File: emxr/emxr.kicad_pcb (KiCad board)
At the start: 2 copper layers, 1 part, among them SW1 Audio Selector

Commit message: finish footprints, starting on component placement
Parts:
- removed SW1: Audio Selector, dba_footprint:CK1050
- added C201: 0.01, Capacitor_THT:C_Disc_D3.8mm_W2.6mm_P2.50mm, F.Cu at (264.2, 22.9)
- added C202: 0.01, Capacitor_THT:C_Disc_D3.8mm_W2.6mm_P2.50mm, F.Cu at (256.5, 39.4)
- added C203: 100p, Capacitor_THT:C_Disc_D5.0mm_W2.5mm_P2.50mm, F.Cu at (252.7, 31.1)
- added C204: 100p, Capacitor_THT:C_Disc_D5.0mm_W2.5mm_P2.50mm, F.Cu at (237.5, 33.0)
- added C205: 22/50, Capacitor_THT:CP_Radial_D5.0mm_P2.00mm, F.Cu at (239.7, 37.5)
- added C206: 22/50, Capacitor_THT:CP_Radial_D5.0mm_P2.00mm, F.Cu at (256.5, 24.5)
- added C207: 100p, Capacitor_THT:C_Disc_D5.0mm_W2.5mm_P2.50mm, F.Cu at (267.3, 33.6)
- added C208: 100p, Capacitor_THT:C_Disc_D5.0mm_W2.5mm_P2.50mm, F.Cu at (276.9, 41.3)
- added C209: 22/50, Capacitor_THT:CP_Radial_D5.0mm_P2.00mm, F.Cu at (269.2, 47.9)
- added C210: 22/50, Capacitor_THT:CP_Radial_D5.0mm_P2.00mm, F.Cu at (269.2, 27.0)
- added C301: 0.1, Capacitor_THT:C_Disc_D3.8mm_W2.6mm_P2.50mm, F.Cu at (250.4, 138.4)
- added C302: 100/25, Capacitor_THT:CP_Radial_D8.0mm_P3.50mm, F.Cu at (256.9, 136.7)
- added C303: 0.1, Capacitor_THT:C_Disc_D3.8mm_W2.6mm_P2.50mm, F.Cu at (239.0, 147.3)
- added C304: 100/25, Capacitor_THT:CP_Radial_D8.0mm_P3.50mm, F.Cu at (231.0, 151.9)
- added C305: 100p, Capacitor_THT:C_Disc_D5.0mm_W2.5mm_P2.50mm, F.Cu at (235.7, 139.2)
- added C306: 22/50, Capacitor_THT:CP_Radial_D5.0mm_P2.00mm, F.Cu at (232.7, 159.1)
- added C307: 220/25, Capacitor_THT:CP_Radial_D10.0mm_P5.00mm, F.Cu at (229.1, 122.7)
- added C308: 100p, Capacitor_THT:C_Disc_D5.0mm_W2.5mm_P2.50mm, F.Cu at (216.9, 149.4)
- added C309: 100p, Capacitor_THT:C_Disc_D5.0mm_W2.5mm_P2.50mm, F.Cu at (235.7, 142.7)
- added C311: 0.001, Capacitor_THT:C_Disc_D3.8mm_W2.6mm_P2.50mm, F.Cu at (239.8, 116.6)
- added C312: 100p, Capacitor_THT:C_Disc_D5.0mm_W2.5mm_P2.50mm, F.Cu at (250.4, 143.8)
- added C313: 22/50, Capacitor_THT:CP_Radial_D5.0mm_P2.00mm, F.Cu at (261.1, 158.6)
- added C314: 220/25, Capacitor_THT:CP_Radial_D10.0mm_P5.00mm, F.Cu at (257.6, 120.7)
- added C315: 100p, Capacitor_THT:C_Disc_D5.0mm_W2.5mm_P2.50mm, F.Cu at (268.2, 139.4)
- added C316: 100p, Capacitor_THT:C_Disc_D5.0mm_W2.5mm_P2.50mm, F.Cu at (247.9, 147.3)
- added C318: 0.001, Capacitor_THT:C_Disc_D3.8mm_W2.6mm_P2.50mm, F.Cu at (246.9, 116.6)
- added C401: 0.01, Capacitor_THT:C_Disc_D3.8mm_W2.6mm_P2.50mm, F.Cu at (66.9, -80.1)
- added C402: 0.01, Capacitor_THT:C_Disc_D3.8mm_W2.6mm_P2.50mm, F.Cu at (29.8, -42.0)
- added C403: 0.01, Capacitor_THT:C_Disc_D3.8mm_W2.6mm_P2.50mm, F.Cu at (51.0, -63.0)
- added C404: 0.01, Capacitor_THT:C_Disc_D3.8mm_W2.6mm_P2.50mm, F.Cu at (45.4, -60.9)
- added C405: 0.01, Capacitor_THT:C_Disc_D3.8mm_W2.6mm_P2.50mm, F.Cu at (57.1, -71.2)
- added C406: 0.01, Capacitor_THT:C_Disc_D3.8mm_W2.6mm_P2.50mm, F.Cu at (41.6, -54.3)
- added C407: 0.01, Capacitor_THT:C_Disc_D3.8mm_W2.6mm_P2.50mm, F.Cu at (30.0, -46.2)
- added C408: 0.01, Capacitor_THT:C_Disc_D3.8mm_W2.6mm_P2.50mm, F.Cu at (56.7, -67.0)
- added C409: 47p, Capacitor_THT:C_Disc_D3.8mm_W2.6mm_P2.50mm, F.Cu at (50.5, -67.1)
- added C410: 150p, Capacitor_THT:C_Disc_D5.0mm_W2.5mm_P2.50mm, F.Cu at (23.7, -42.2)
- added C411: 150p, Capacitor_THT:C_Disc_D5.0mm_W2.5mm_P2.50mm, F.Cu at (17.1, -42.2)
- added C412: 220/25, Capacitor_THT:CP_Radial_D10.0mm_P5.00mm, F.Cu at (40.7, -68.7)
- added C413: 22/50, Capacitor_THT:CP_Radial_D5.0mm_P2.00mm, F.Cu at (24.1, -47.5)
- added C414: 22/50, Capacitor_THT:CP_Radial_D5.0mm_P2.00mm, F.Cu at (54.4, -83.0)
- added C415: 22/50, Capacitor_THT:CP_Radial_D5.0mm_P2.00mm, F.Cu at (54.4, -76.5)
- added C416: 220p, Capacitor_THT:C_Disc_D5.0mm_W2.5mm_P2.50mm, F.Cu at (60.7, -77.8)
- added C417: 47/50, Capacitor_THT:CP_Radial_D6.3mm_P2.50mm, F.Cu at (28.3, -58.4)
- added C418: 100p, Capacitor_THT:C_Disc_D5.0mm_W2.5mm_P2.50mm, F.Cu at (30.4, -50.3)
- added C420: 47p, Capacitor_THT:C_Disc_D3.8mm_W2.6mm_P2.50mm, F.Cu at (66.9, -84.2)
- added C421: 150p, Capacitor_THT:C_Disc_D5.0mm_W2.5mm_P2.50mm, F.Cu at (51.0, -71.2)
- added C422: 150p, Capacitor_THT:C_Disc_D5.0mm_W2.5mm_P2.50mm, F.Cu at (-10.9, -40.0)
- added C423: 220/25, Capacitor_THT:CP_Radial_D10.0mm_P5.00mm, F.Cu at (17.2, -56.5)
- added C424: 22/50, Capacitor_THT:CP_Radial_D5.0mm_P2.00mm, F.Cu at (61.0, -83.0)
- added C425: 22/50, Capacitor_THT:CP_Radial_D5.0mm_P2.00mm, F.Cu at (17.5, -47.5)
- added C426: 22/50, Capacitor_THT:CP_Radial_D5.0mm_P2.00mm, F.Cu at (39.5, -59.6)
- added C427: 220p, Capacitor_THT:C_Disc_D5.0mm_W2.5mm_P2.50mm, F.Cu at (35.5, -54.4)
- added C428: 47/50, Capacitor_THT:CP_Radial_D6.3mm_P2.50mm, F.Cu at (9.96, -42.2)
- added C429: 100p, Capacitor_THT:C_Disc_D5.1mm_W3.2mm_P5.00mm, F.Cu at (0.57, -43.8)
- added FR301: 10 1/4, Resistor_THT:R_Axial_DIN0207_L6.3mm_D2.5mm_P5.08mm_Vertical, F.Cu at (258.9, 130.6)
- added FR302: 10 1/4, Resistor_THT:R_Axial_DIN0207_L6.3mm_D2.5mm_P5.08mm_Vertical, F.Cu at (244.1, 151.9)
- added IC201: NJM4558D, Package_DIP:DIP-8_W7.62mm_Socket_LongPads, F.Cu at (256.5, 28.6)
- added IC301: NJM4556D, Package_DIP:DIP-8_W7.62mm_Socket_LongPads, F.Cu at (239.5, 136.4)
- added IC401: NJM2068DD, Package_DIP:DIP-8_W7.62mm_Socket_LongPads, F.Cu at (15.7, -72.0)
- added IC402: NJM4580, Package_DIP:DIP-8_W7.62mm_Socket_LongPads, F.Cu at (42.4, -84.2)
- added IC403: NJM2068DD, Package_DIP:DIP-8_W7.62mm_Socket_LongPads, F.Cu at (27.5, -72.0)
- added IC404: NJM4580, Package_DIP:DIP-8_W7.62mm_Socket_LongPads, F.Cu at (2.43, -55.9)
- added J101: POWER, Connector_JST:JST_XH_B4B-XH-A_1x04_P2.50mm_Vertical, F.Cu at (-18.5, -117.4)
- added J102: DSP_PW, Connector_JST:JST_XH_B5B-XH-A_1x05_P2.50mm_Vertical, F.Cu at (-35.5, -117.4)
- added J103: Bus Conn, Connector_PinHeader_2.54mm:PinHeader_1x12_P2.54mm_Vertical, F.Cu at (-41.3, -118.4)
- added J104: GEQ_L_PRE, Connector_JST:JST_XH_B3B-XH-A_1x03_P2.50mm_Vertical, F.Cu at (-4.08, -117.4)
- added J105: GEQ_L_POST, Connector_JST:JST_XH_B3B-XH-A_1x03_P2.50mm_Vertical, F.Cu at (-35.5, -101.8)
- added J106: GEQ_R_PRE, Connector_JST:JST_XH_B2B-XH-A_1x02_P2.50mm_Vertical, F.Cu at (-35.5, -94.0)
- added J107: GEQ_R_POST, Connector_JST:JST_XH_B2B-XH-A_1x02_P2.50mm_Vertical, F.Cu at (-23.5, -101.8)
- added J108: AUDIO_OUT, Connector_JST:JST_XH_B4B-XH-A_1x04_P2.50mm_Vertical, F.Cu at (-35.5, -109.6)
- added J201: RCA_IN_A_B, Connector_JST:JST_XH_B6B-XH-A_1x06_P2.50mm_Vertical, F.Cu at (-44.7, 42.0)
- added J202: RCA_IN_3_4, Connector_JST:JST_XH_B6B-XH-A_1x06_P2.50mm_Vertical, F.Cu at (-45.6, 73.3)
- added J203: AUX1_IN, Connector_JST:JST_XH_B3B-XH-A_1x03_P2.50mm_Vertical, F.Cu at (-44.4, 91.9)
- added J204: AUX2_IN, Connector_JST:JST_XH_B3B-XH-A_1x03_P2.50mm_Vertical, F.Cu at (-45.7, 84.9)
- added J205: InpVolL, Connector_JST:JST_XH_B3B-XH-A_1x03_P2.50mm_Vertical, F.Cu at (232.4, 32.5)
- added J206: InpVolR, Connector_JST:JST_XH_B2B-XH-A_1x02_P2.50mm_Vertical, F.Cu at (271.7, 40.6)
- added J207: SrcInL, Connector_JST:JST_XH_B6B-XH-A_1x06_P2.50mm_Vertical, F.Cu at (-36.1, 61.0)
- added J208: SrcSel, Connector_JST:JST_XH_B2B-XH-A_1x02_P2.50mm_Vertical, F.Cu at (247.7, 42.5)
- added J209: SrcInR, Connector_JST:JST_XH_B6B-XH-A_1x06_P2.50mm_Vertical, F.Cu at (-36.1, 41.3)
- added J301: HPHONES, Connector_JST:JST_XH_B3B-XH-A_1x03_P2.50mm_Vertical, F.Cu at (240.8, 108.7)
- added J302: HPVolL, Connector_JST:JST_XH_B3B-XH-A_1x03_P2.50mm_Vertical, F.Cu at (243.8, 160.5)
- added J303: HPVolR, Connector_JST:JST_XH_B2B-XH-A_1x02_P2.50mm_Vertical, F.Cu at (252.0, 159.5)
- added J401: FrontVolL, Connector_JST:JST_XH_B3B-XH-A_1x03_P2.50mm_Vertical, F.Cu at (30.4, -78.9)
- added J402: FrontVolR, Connector_JST:JST_XH_B3B-XH-A_1x03_P2.50mm_Vertical, F.Cu at (-9.48, -46.5)
- added LC301: 270p, dba_footprint:LCL_EMX, F.Cu at (236.2, 111.3)
- added LC302: 270p, dba_footprint:LCL_EMX, F.Cu at (250.4, 111.3)
- added R101: 10, Resistor_THT:R_Axial_DIN0207_L6.3mm_D2.5mm_P10.16mm_Horizontal, F.Cu at (-42.0, -86.1)
- added R102: 10, Resistor_THT:R_Axial_DIN0207_L6.3mm_D2.5mm_P10.16mm_Horizontal, F.Cu at (-22.9, -110.9)
- added R201: 15k, Resistor_THT:R_Axial_DIN0207_L6.3mm_D2.5mm_P10.16mm_Horizontal, F.Cu at (239.4, 29.8)
- added R202: 100, Resistor_THT:R_Axial_DIN0207_L6.3mm_D2.5mm_P10.16mm_Horizontal, F.Cu at (222.2, 29.8)
- added R203: 47k, Resistor_THT:R_Axial_DIN0207_L6.3mm_D2.5mm_P10.16mm_Horizontal, F.Cu at (226.1, 40.0)
- added R204: 100, Resistor_THT:R_Axial_DIN0207_L6.3mm_D2.5mm_P10.16mm_Horizontal, F.Cu at (243.2, 37.5)
- added R205: 27k, Resistor_THT:R_Axial_DIN0207_L6.3mm_D2.5mm_P10.16mm_Horizontal, F.Cu at (246.4, 15.9)
- added R206: 47k, Resistor_THT:R_Axial_DIN0207_L6.3mm_D2.5mm_P10.16mm_Horizontal, F.Cu at (256.5, 19.1)
- added R207: 10k, Resistor_THT:R_Axial_DIN0207_L6.3mm_D2.5mm_P10.16mm_Horizontal, F.Cu at (239.4, 26.0)
- added R208: 18k, Resistor_THT:R_Axial_DIN0207_L6.3mm_D2.5mm_P10.16mm_Horizontal, F.Cu at (253.4, 34.3)
- added R209: 15k, Resistor_THT:R_Axial_DIN0207_L6.3mm_D2.5mm_P10.16mm_Horizontal, F.Cu at (280.7, 31.1)
- added R210: 100, Resistor_THT:R_Axial_DIN0207_L6.3mm_D2.5mm_P10.16mm_Horizontal, F.Cu at (273.7, 45.1)
- added R211: 47k, Resistor_THT:R_Axial_DIN0207_L6.3mm_D2.5mm_P10.16mm_Horizontal, F.Cu at (276.9, 55.2)
- added R212: 100, Resistor_THT:R_Axial_DIN0207_L6.3mm_D2.5mm_P10.16mm_Horizontal, F.Cu at (264.2, 49.5)
- added R213: 27k, Resistor_THT:R_Axial_DIN0207_L6.3mm_D2.5mm_P10.16mm_Horizontal, F.Cu at (259.1, 19.1)
- added R214: 18k, Resistor_THT:R_Axial_DIN0207_L6.3mm_D2.5mm_P10.16mm_Horizontal, F.Cu at (261.0, 39.4)
- added R215: 47k, Resistor_THT:R_Axial_DIN0207_L6.3mm_D2.5mm_P10.16mm_Horizontal, F.Cu at (269.2, 15.8)
- added R216: 10k, Resistor_THT:R_Axial_DIN0207_L6.3mm_D2.5mm_P10.16mm_Horizontal, F.Cu at (280.7, 34.9)
- added R301: 10k, Resistor_THT:R_Axial_DIN0207_L6.3mm_D2.5mm_P10.16mm_Horizontal, F.Cu at (231.6, 146.3)
- added R302: 100, Resistor_THT:R_Axial_DIN0207_L6.3mm_D2.5mm_P10.16mm_Horizontal, F.Cu at (235.7, 165.6)
- added R303: 220, Resistor_THT:R_Axial_DIN0207_L6.3mm_D2.5mm_P10.16mm_Horizontal, F.Cu at (220.5, 136.1)
- added R304: 220, Resistor_THT:R_Axial_DIN0207_L6.3mm_D2.5mm_P10.16mm_Horizontal, F.Cu at (224.0, 146.3)
- added R305: 100/1W, Resistor_THT:R_Axial_DIN0207_L6.3mm_D2.5mm_P15.24mm_Horizontal, F.Cu at (236.2, 133.1)
- added R306: 18k, Resistor_THT:R_Axial_DIN0207_L6.3mm_D2.5mm_P10.16mm_Horizontal, F.Cu at (216.9, 146.3)
- added R307: 100k, Resistor_THT:R_Axial_DIN0207_L6.3mm_D2.5mm_P10.16mm_Horizontal, F.Cu at (239.8, 118.9)
- added R308: 10k, Resistor_THT:R_Axial_DIN0207_L6.3mm_D2.5mm_P10.16mm_Horizontal, F.Cu at (227.6, 146.3)
- added R309: 10k, Resistor_THT:R_Axial_DIN0207_L6.3mm_D2.5mm_P10.16mm_Horizontal, F.Cu at (254.0, 152.4)
- added R310: 100, Resistor_THT:R_Axial_DIN0207_L6.3mm_D2.5mm_P10.16mm_Horizontal, F.Cu at (248.9, 165.6)
- added R311: 220, Resistor_THT:R_Axial_DIN0207_L6.3mm_D2.5mm_P10.16mm_Horizontal, F.Cu at (264.7, 152.4)
- added R312: 220, Resistor_THT:R_Axial_DIN0207_L6.3mm_D2.5mm_P10.16mm_Horizontal, F.Cu at (261.1, 142.2)
- added R313: 100/1W, Resistor_THT:R_Axial_DIN0207_L6.3mm_D2.5mm_P15.24mm_Horizontal, F.Cu at (250.4, 133.1)
- added R314: 18k, Resistor_THT:R_Axial_DIN0207_L6.3mm_D2.5mm_P10.16mm_Horizontal, F.Cu at (268.2, 142.2)
- added R315: 100k, Resistor_THT:R_Axial_DIN0207_L6.3mm_D2.5mm_P10.16mm_Horizontal, F.Cu at (246.9, 118.9)
- added R316: 10k, Resistor_THT:R_Axial_DIN0207_L6.3mm_D2.5mm_P10.16mm_Horizontal, F.Cu at (257.6, 152.4)
- added R401: 27k, Resistor_THT:R_Axial_DIN0207_L6.3mm_D2.5mm_P10.16mm_Horizontal, F.Cu at (1.93, -64.0)
- added R402: 10k, Resistor_THT:R_Axial_DIN0207_L6.3mm_D2.5mm_P10.16mm_Horizontal, F.Cu at (15.2, -80.2)
- added R403: 11k, Resistor_THT:R_Axial_DIN0207_L6.3mm_D2.5mm_P10.16mm_Horizontal, F.Cu at (-11.4, -51.9)
- added R404: 10k, Resistor_THT:R_Axial_DIN0207_L6.3mm_D2.5mm_P10.16mm_Horizontal, F.Cu at (-11.4, -60.0)
- added R405: 100k, Resistor_THT:R_Axial_DIN0207_L6.3mm_D2.5mm_P10.16mm_Horizontal, F.Cu at (15.2, -84.3)
- added R406: 100, Resistor_THT:R_Axial_DIN0207_L6.3mm_D2.5mm_P10.16mm_Horizontal, F.Cu at (1.93, -76.2)
- added R407: 330, Resistor_THT:R_Axial_DIN0207_L6.3mm_D2.5mm_P10.16mm_Horizontal, F.Cu at (1.93, -72.2)
- added R408: 10, Resistor_THT:R_Axial_DIN0207_L6.3mm_D2.5mm_P10.16mm_Horizontal, F.Cu at (1.93, -84.3)
- added R409: 47k, Resistor_THT:R_Axial_DIN0207_L6.3mm_D2.5mm_P10.16mm_Horizontal, F.Cu at (1.93, -68.1)
- added R410: 15k, Resistor_THT:R_Axial_DIN0207_L6.3mm_D2.5mm_P10.16mm_Horizontal, F.Cu at (-11.4, -76.2)
- added R411: 27k, Resistor_THT:R_Axial_DIN0207_L6.3mm_D2.5mm_P10.16mm_Horizontal, F.Cu at (1.93, -80.2)
- added R412: 10k, Resistor_THT:R_Axial_DIN0207_L6.3mm_D2.5mm_P10.16mm_Horizontal, F.Cu at (28.6, -84.3)
- added R413: 11k, Resistor_THT:R_Axial_DIN0207_L6.3mm_D2.5mm_P10.16mm_Horizontal, F.Cu at (-11.4, -56.0)
- added R414: 10k, Resistor_THT:R_Axial_DIN0207_L6.3mm_D2.5mm_P10.16mm_Horizontal, F.Cu at (15.2, -76.2)
- added R415: 100k, Resistor_THT:R_Axial_DIN0207_L6.3mm_D2.5mm_P10.16mm_Horizontal, F.Cu at (-11.4, -64.0)
- added R416: 100, Resistor_THT:R_Axial_DIN0207_L6.3mm_D2.5mm_P10.16mm_Horizontal, F.Cu at (-11.4, -68.1)
- added R417: 330, Resistor_THT:R_Axial_DIN0207_L6.3mm_D2.5mm_P10.16mm_Horizontal, F.Cu at (-11.4, -80.2)
- added R418: 10, Resistor_THT:R_Axial_DIN0207_L6.3mm_D2.5mm_P10.16mm_Horizontal, F.Cu at (-11.4, -84.3)
- added R419: 47k, Resistor_THT:R_Axial_DIN0207_L6.3mm_D2.5mm_P10.16mm_Horizontal, F.Cu at (1.93, -60.0)
- added R420: 15k, Resistor_THT:R_Axial_DIN0207_L6.3mm_D2.5mm_P10.16mm_Horizontal, F.Cu at (-11.4, -72.2)
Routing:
- added copper zone on B.Cu, net GND
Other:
- board text removed: "BACK"
- board text removed: "FRONT"

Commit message: progress on layouting
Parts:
- moved J106 331.9 mm to (246.9, 80.5)
- moved J101 275.3 mm to (52.8, 148.5), turned to 90 degrees
- moved J104 249.6 mm to (144.3, 83.4), turned to -90 degrees
- moved C424 240.8 mm to (262.9, 48.3)
- moved C427 240.8 mm to (237.4, 77.0)
- moved C403 240.8 mm to (252.9, 68.4)
- moved C404 240.8 mm to (247.2, 70.5)
- moved C407 240.8 mm to (231.8, 85.1)
- moved C408 240.8 mm to (258.6, 64.3)
- moved C420 240.8 mm to (268.8, 47.1)
- moved C421 240.8 mm to (252.9, 60.1)
- moved C422 240.8 mm to (190.9, 91.3)
- moved C425 240.8 mm to (219.4, 83.8)
- moved C426 240.8 mm to (241.4, 71.7)
- moved C428 240.8 mm to (211.8, 89.1)
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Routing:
- net Net-(C411-Pad1): track 0.00 -> 30.0 mm
- net SINGAL_L_PRE_GEQ: track 0.00 -> 29.5 mm
- net Net-(C410-Pad2): track 0.00 -> 28.2 mm
- net Net-(C418-Pad1): track 0.00 -> 24.5 mm
- net Net-(C409-Pad1): track 0.00 -> 23.1 mm
- net Net-(C410-Pad1): track 0.00 -> 17.8 mm
- net Net-(C411-Pad2): track 0.00 -> 16.7 mm
- net Net-(C409-Pad2): track 0.00 -> 13.1 mm
- net /Stereo/POT_FRONT_VOL_L_PRE: track 0.00 -> 9.42 mm
- net /Stereo/POT_FRONT_VOL_L_POST: track 0.00 -> 9.18 mm
- net -15V: track 0.00 -> 6.73 mm
- net +15V: track 0.00 -> 6.60 mm
- net Net-(C415-Pad1): track 0.00 -> 6.39 mm
- net Net-(C417-Pad2): track 0.00 -> 6.14 mm
- net Net-(C417-Pad1): track 0.00 -> 5.98 mm
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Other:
- board text added: "JLCJLCJLCJLC"

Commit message: replicated layout
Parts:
- removed C403, C404, C407, C408: 0.01, Capacitor_THT:C_Disc_D3.8mm_W2.6mm_P2.50mm
- removed C420: 47p, Capacitor_THT:C_Disc_D3.8mm_W2.6mm_P2.50mm
- removed C421, C422: 150p, Capacitor_THT:C_Disc_D5.0mm_W2.5mm_P2.50mm
- removed C423: 220/25, Capacitor_THT:CP_Radial_D10.0mm_P5.00mm
- removed C424, C425, C426: 22/50, Capacitor_THT:CP_Radial_D5.0mm_P2.00mm
- removed C427: 220p, Capacitor_THT:C_Disc_D5.0mm_W2.5mm_P2.50mm
- removed C428: 47/50, Capacitor_THT:CP_Radial_D6.3mm_P2.50mm
- removed C429: 100p, Capacitor_THT:C_Disc_D5.1mm_W3.2mm_P5.00mm
- removed IC403: NJM2068DD, Package_DIP:DIP-8_W7.62mm_Socket_LongPads
- removed IC404: NJM4580, Package_DIP:DIP-8_W7.62mm_Socket_LongPads
- removed J402: FrontVolR, Connector_JST:JST_XH_B3B-XH-A_1x03_P2.50mm_Vertical
- removed R411: 27k, Resistor_THT:R_Axial_DIN0207_L6.3mm_D2.5mm_P10.16mm_Horizontal
- removed R412, R414: 10k, Resistor_THT:R_Axial_DIN0207_L6.3mm_D2.5mm_P10.16mm_Horizontal
- removed R413: 11k, Resistor_THT:R_Axial_DIN0207_L6.3mm_D2.5mm_P10.16mm_Horizontal
- removed R415: 100k, Resistor_THT:R_Axial_DIN0207_L6.3mm_D2.5mm_P10.16mm_Horizontal
- removed R416: 100, Resistor_THT:R_Axial_DIN0207_L6.3mm_D2.5mm_P10.16mm_Horizontal
- removed R417: 330, Resistor_THT:R_Axial_DIN0207_L6.3mm_D2.5mm_P10.16mm_Horizontal
- removed R418: 10, Resistor_THT:R_Axial_DIN0207_L6.3mm_D2.5mm_P10.16mm_Horizontal
- removed R419: 47k, Resistor_THT:R_Axial_DIN0207_L6.3mm_D2.5mm_P10.16mm_Horizontal
- removed R420: 15k, Resistor_THT:R_Axial_DIN0207_L6.3mm_D2.5mm_P10.16mm_Horizontal
- added C501: 0.01, Capacitor_THT:C_Disc_D3.8mm_W2.6mm_P2.50mm, F.Cu at (199.7, 124.5)
- added C502: 0.01, Capacitor_THT:C_Disc_D3.8mm_W2.6mm_P2.50mm, F.Cu at (218.0, 120.9)
- added C503: 0.01, Capacitor_THT:C_Disc_D3.8mm_W2.6mm_P2.50mm, F.Cu at (194.6, 110.2)
- added C504: 0.01, Capacitor_THT:C_Disc_D3.8mm_W2.6mm_P2.50mm, F.Cu at (212.6, 106.7)
- added C505: 47p, Capacitor_THT:C_Disc_D3.8mm_W2.6mm_P2.50mm, F.Cu at (199.7, 110.2)
- added C506: 150p, Capacitor_THT:C_Disc_D5.0mm_W2.5mm_P2.50mm, F.Cu at (218.0, 106.7)
- added C507: 150p, Capacitor_THT:C_Disc_D5.0mm_W2.5mm_P2.50mm, F.Cu at (212.6, 120.9)
- added C508: 220/25, Capacitor_THT:CP_Radial_D10.0mm_P5.00mm, F.Cu at (187.7, 105.1)
- added C509: 22/50, Capacitor_THT:CP_Radial_D5.0mm_P2.00mm, F.Cu at (207.5, 116.0)
- added C510: 22/50, Capacitor_THT:CP_Radial_D5.0mm_P2.00mm, F.Cu at (239.8, 102.6)
- added C511: 22/50, Capacitor_THT:CP_Radial_D5.0mm_P2.00mm, F.Cu at (239.8, 110.7)
- added C512: 220p, Capacitor_THT:C_Disc_D5.0mm_W2.5mm_P2.50mm, F.Cu at (194.8, 104.9)
- added C513: 47/50, Capacitor_THT:CP_Radial_D6.3mm_P2.50mm, F.Cu at (240.3, 122.5)
- added C514: 100p, Capacitor_THT:C_Disc_D5.0mm_W2.5mm_P2.50mm, F.Cu at (206.8, 120.9)
- added IC501: NJM2068DD, Package_DIP:DIP-8_W7.62mm_Socket_LongPads, F.Cu at (202.2, 113.5)
- added IC502: NJM4580, Package_DIP:DIP-8_W7.62mm_Socket_LongPads, F.Cu at (220.5, 110.0)
- added J501: FrontVolL, Connector_JST:JST_XH_B3B-XH-A_1x03_P2.50mm_Vertical, F.Cu at (248.4, 106.5)
- added R501: 27k, Resistor_THT:R_Axial_DIN0207_L6.3mm_D2.5mm_P10.16mm_Horizontal, F.Cu at (193.0, 100.8)
- added R502: 10k, Resistor_THT:R_Axial_DIN0207_L6.3mm_D2.5mm_P10.16mm_Horizontal, F.Cu at (212.1, 100.8)
- added R503: 11k, Resistor_THT:R_Axial_DIN0207_L6.3mm_D2.5mm_P10.16mm_Horizontal, F.Cu at (234.4, 118.9)
- added R504: 10k, Resistor_THT:R_Axial_DIN0207_L6.3mm_D2.5mm_P10.16mm_Horizontal, F.Cu at (207.5, 111.0)
- added R505: 100, Resistor_THT:R_Axial_DIN0207_L6.3mm_D2.5mm_P10.16mm_Horizontal, F.Cu at (234.4, 108.2)
- added R506: 100k, Resistor_THT:R_Axial_DIN0207_L6.3mm_D2.5mm_P10.16mm_Horizontal, F.Cu at (234.4, 104.6)
- added R507: 330, Resistor_THT:R_Axial_DIN0207_L6.3mm_D2.5mm_P10.16mm_Horizontal, F.Cu at (224.3, 122.2)
- added R508: 10, Resistor_THT:R_Axial_DIN0207_L6.3mm_D2.5mm_P10.16mm_Horizontal, F.Cu at (234.4, 125.7)
- added R509: 47k, Resistor_THT:R_Axial_DIN0207_L6.3mm_D2.5mm_P10.16mm_Horizontal, F.Cu at (234.4, 111.8)
- added R510: 15k, Resistor_THT:R_Axial_DIN0207_L6.3mm_D2.5mm_P10.16mm_Horizontal, F.Cu at (234.4, 115.3)
- moved C204 150.5 mm to (169.0, -30.4)
- moved C208 150.5 mm to (208.4, -22.1)
- moved C209 150.5 mm to (200.8, -15.4)
- moved C210 150.5 mm to (200.8, -36.4)
- moved J206 150.5 mm to (203.3, -22.7)
- moved R202 150.5 mm to (153.8, -33.5)
- moved R203 150.5 mm to (157.6, -23.4)
- moved R205 150.5 mm to (177.9, -47.5)
- moved R208 150.5 mm to (184.9, -29.1)
- moved R209 150.5 mm to (212.2, -32.3)
- moved R210 150.5 mm to (205.2, -18.3)
- moved R211 150.5 mm to (208.4, -8.13)
- moved R214 150.5 mm to (192.5, -24.0)
- moved R215 150.5 mm to (200.8, -47.6)
- moved R216 150.5 mm to (212.2, -28.4)
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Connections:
- net /Stereo/POT_FRONT_VOL_L_POST renamed /Stereo Channel L/POT_FRONT_VOL_L_POST
- net /Stereo/POT_FRONT_VOL_L_PRE renamed /Stereo Channel L/POT_FRONT_VOL_L_PRE
- J201 pad 3: /Audio Selection/RCA_IN_A_R -> /Audio Selection/RCA_IN_B_L
- J201 pad 4: /Audio Selection/RCA_IN_B_L -> /Audio Selection/RCA_IN_A_R
- J202 pad 3: /Audio Selection/RCA_IN_C_R -> /Audio Selection/RCA_IN_D_L
- J202 pad 4: /Audio Selection/RCA_IN_D_L -> /Audio Selection/RCA_IN_C_R
- J207 pad 5: /Audio Selection/AUX_IN_L -> /Audio Selection/AUX1_IN_L
- J209 pad 5: /Audio Selection/AUX_IN_R -> /Audio Selection/AUX1_IN_R
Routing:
- net Net-(C507-Pad1): track 0.00 -> 30.0 mm
- net Net-(C506-Pad2): track 0.00 -> 28.2 mm
- net SINGAL_R_PRE_GEQ: track 0.00 -> 27.3 mm
- net Net-(C514-Pad1): track 0.00 -> 24.5 mm
- net Net-(C505-Pad1): track 0.00 -> 23.1 mm
- net Net-(C505-Pad2): track 0.00 -> 19.5 mm
- net Net-(C506-Pad1): track 0.00 -> 17.8 mm
- net Net-(C507-Pad2): track 0.00 -> 16.7 mm
- net /Stereo Channel R/POT_FRONT_VOL_L_PRE: track 0.00 -> 14.8 mm
- net /Stereo Channel R/POT_FRONT_VOL_L_POST: track 0.00 -> 9.18 mm
- net -15V: track 6.73 -> 13.5 mm
- net +15V: track 6.60 -> 13.2 mm
- net Net-(C511-Pad1): track 0.00 -> 6.39 mm
- net Net-(C409-Pad2): track 13.1 -> 19.5 mm
- net Net-(C513-Pad2): track 0.00 -> 6.14 mm
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
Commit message: more routing and reshuffling
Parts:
- removed J102: DSP_PW, Connector_JST:JST_XH_B5B-XH-A_1x05_P2.50mm_Vertical
- J103: footprint Connector_PinHeader_2.54mm:PinHeader_1x12_P2.54mm_Vertical -> Connector_JST:JST_XH_B6B-XH-A_1x06_P2.50mm_Vertical
- moved J103 321.2 mm to (117.0, 161.1), turned to 180 degrees
- moved R101 297.3 mm to (213.2, 66.3), turned to 180 degrees
- moved J105 295.9 mm to (211.9, 60.5)
- moved J108 288.8 mm to (198.0, 60.5)
- moved R102 277.3 mm to (190.3, 66.3)
- moved J107 267.4 mm to (189.1, 60.5)
- moved C206 205.4 mm to (113.0, 152.3)
- moved R206 204.9 mm to (113.0, 146.3), turned to 0 degrees
- moved J205 202.1 mm to (86.9, 155.9), turned to 90 degrees
- moved C201 198.2 mm to (93.5, 129.3), turned to 90 degrees
- moved R205 198.0 mm to (123.2, 142.7), turned to 180 degrees
- moved C205 196.7 mm to (96.8, 156.2)
- moved C204 196.7 mm to (93.7, 151.4), turned to 90 degrees
- moved R204 193.9 mm to (96.8, 151.6)
- moved R208 193.8 mm to (106.9, 148.3)
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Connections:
- J103 pad 2: +15VD -> -15V
- J103 pad 3: -15VD -> +15V
- J103 pad 4: GND -> BUS_R
- J103 pad 5: unconnected-(J103-Pad5) -> BUS_L
- J108 pad 1: SINGAL_L_POST_GEQ -> SINGAL_R_POST_GEQ
- J108 pad 3: SINGAL_R_POST_GEQ -> GND
- J108 pad 4: GND -> SINGAL_L_POST_GEQ
- J205 pad 1: Net-(C204-Pad1) -> Net-(C205-Pad2)
- J205 pad 3: Net-(C205-Pad2) -> Net-(C204-Pad1)
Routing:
- net BUS_R: track 0.00 -> 61.6 mm
- net BUS_L: track 0.00 -> 39.0 mm
- net Net-(C203-Pad2): track 0.00 -> 31.5 mm
- net +15V: track 13.2 -> 38.0 mm
- net Net-(C207-Pad2): track 0.00 -> 24.3 mm
- net Net-(IC201-Pad3): track 0.00 -> 23.0 mm
- net Net-(IC201-Pad5): track 0.00 -> 19.2 mm
- net -15V: track 13.5 -> 31.3 mm
- net Net-(C203-Pad1): track 0.00 -> 16.0 mm
- net Net-(C204-Pad1): track 0.00 -> 14.8 mm
- net Net-(C207-Pad1): track 0.00 -> 12.3 mm
- net Net-(C208-Pad1): track 0.00 -> 12.2 mm
- net PHANTOM_PW: track 0.00 -> 10.5 mm
- net Net-(C205-Pad2): track 0.00 -> 8.11 mm
- net Net-(C206-Pad2): track 0.00 -> 7.59 mm
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
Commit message: first pcb draft
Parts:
- removed J201: RCA_IN_A_B, Connector_JST:JST_XH_B6B-XH-A_1x06_P2.50mm_Vertical
- removed J202: RCA_IN_3_4, Connector_JST:JST_XH_B6B-XH-A_1x06_P2.50mm_Vertical
- removed J203: AUX1_IN, Connector_JST:JST_XH_B3B-XH-A_1x03_P2.50mm_Vertical
- removed J204: AUX2_IN, Connector_JST:JST_XH_B3B-XH-A_1x03_P2.50mm_Vertical
- removed J207: SrcInL, Connector_JST:JST_XH_B6B-XH-A_1x06_P2.50mm_Vertical
- removed J209: SrcInR, Connector_JST:JST_XH_B6B-XH-A_1x06_P2.50mm_Vertical
- added H101: MH, MountingHole:MountingHole_3.2mm_M3_DIN965_Pad_TopBottom, F.Cu at (74.9, 94.7)
- added H102: MH, MountingHole:MountingHole_3.2mm_M3_DIN965_Pad_TopBottom, F.Cu at (225.6, 94.2)
- added H103: MH, MountingHole:MountingHole_3.2mm_M3_DIN965_Pad_TopBottom, F.Cu at (226.1, 160.3)
- added H104: MH, MountingHole:MountingHole_3.2mm_M3_DIN965_Pad_TopBottom, F.Cu at (75.7, 161.5)
- moved C308 202.4 mm to (81.0, 129.5), turned to 0 degrees
- moved R306 201.8 mm to (80.9, 122.4), turned to 0 degrees
- moved R304 194.9 mm to (80.9, 126.0), turned to 0 degrees
- moved C307 193.4 mm to (80.6, 103.6), turned to 0 degrees
- moved C306 190.8 mm to (76.6, 116.6), turned to 180 degrees
- moved R302 190.0 mm to (77.1, 132.6), turned to 90 degrees
- moved J302 188.3 mm to (67.7, 112.5), turned to 90 degrees
- moved R303 188.2 mm to (91.1, 118.9), turned to 180 degrees
- moved J303 185.6 mm to (67.7, 155.4), turned to 90 degrees
- moved C304 182.1 mm to (88.2, 136.1), turned to 0 degrees
- moved LC301 179.4 mm to (91.4, 101.1), turned to 90 degrees
- moved R308 177.6 mm to (94.4, 117.3), turned to 0 degrees
- moved R310 177.6 mm to (77.1, 135.1), turned to -90 degrees
- moved R305 173.8 mm to (90.6, 111.3), turned to 180 degrees
- moved R301 173.6 mm to (94.4, 120.9), turned to 0 degrees
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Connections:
- J104 pad 1: SINGAL_L_PRE_GEQ -> GND
- J104 pad 3: GND -> SINGAL_L_PRE_GEQ
- J303 pad 1: Net-(J303-Pad1) -> Net-(C313-Pad2)
- J303 pad 2: Net-(C313-Pad2) -> Net-(R310-Pad2)
- R310 pad 2: Net-(J303-Pad1) -> Net-(R310-Pad2)
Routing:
- net -15V: track 31.3 -> 257.5 mm, vias 0 -> 8
- net +15V: track 38.0 -> 170.6 mm
- net Net-(C312-Pad2): track 0.00 -> 50.2 mm
- net Net-(C305-Pad2): track 0.00 -> 28.6 mm
- net Net-(C305-Pad1): track 0.00 -> 17.4 mm
- net Net-(C303-Pad1): track 0.00 -> 16.6 mm
- net Net-(C313-Pad1): track 0.00 -> 16.6 mm
- net Net-(C306-Pad1): track 0.00 -> 15.5 mm
- net Net-(C312-Pad1): track 0.00 -> 14.8 mm
- net Net-(J302-Pad1): track 0.00 -> 14.7 mm
- net Net-(C301-Pad2): track 0.00 -> 14.4 mm
- net Net-(R310-Pad2): track 0.00 -> 13.3 mm
- net Net-(C306-Pad2): track 0.00 -> 12.0 mm
- net Net-(C307-Pad2): track 0.00 -> 11.9 mm
- net Net-(C314-Pad2): track 0.00 -> 11.1 mm
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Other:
- board outline added: 167.9 x 76.5 mm

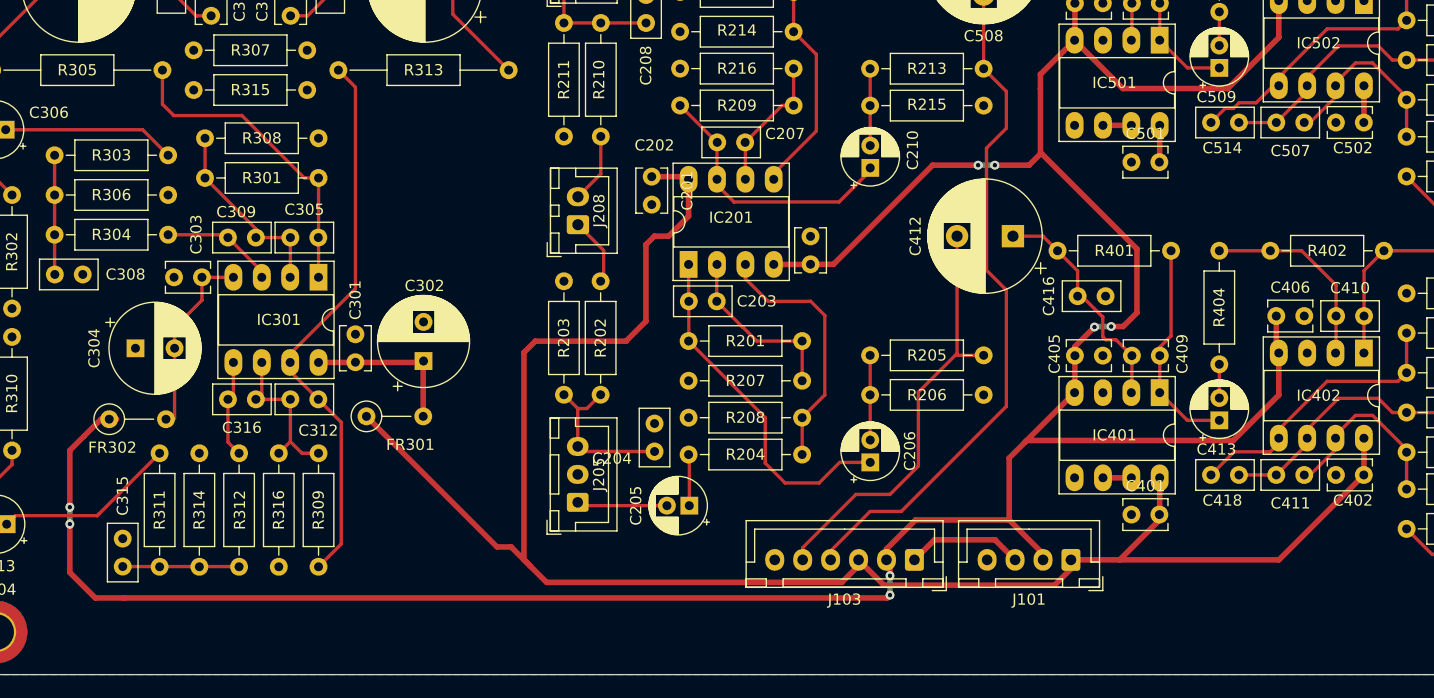
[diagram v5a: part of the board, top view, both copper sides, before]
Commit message: fix some missing routes in pcb
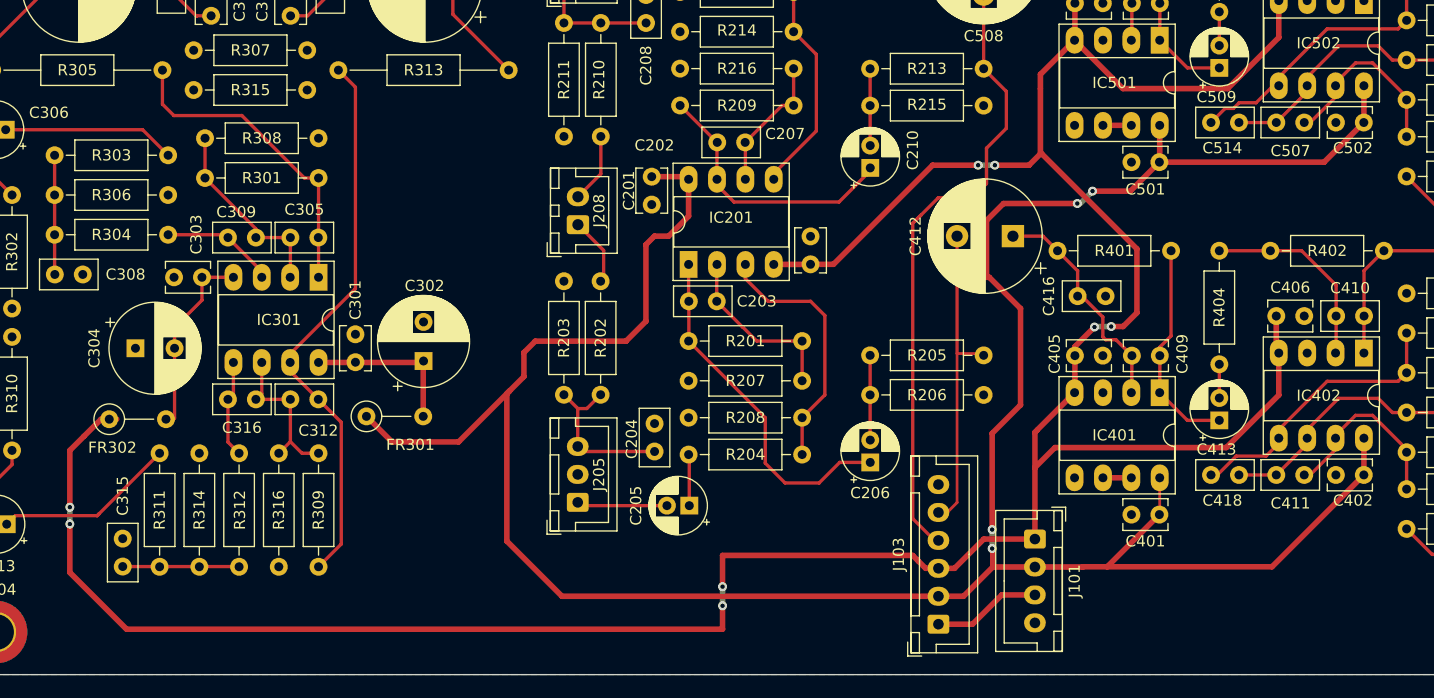
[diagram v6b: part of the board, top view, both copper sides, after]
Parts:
- moved J103 6.15 mm to (160.0, 160.8), turned to 90 degrees
- moved J101 3.72 mm to (168.7, 153.2), turned to -90 degrees
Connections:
- J101 pad 1: +15V -> -15V
- J101 pad 2: -15V -> +15V
- J103 pad 2: -15V -> +15V
- J103 pad 3: +15V -> -15V
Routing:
- net +15V: track 170.6 -> 238.1 mm, vias 0 -> 4
- net BUS_L: track 39.0 -> 28.3 mm
- net BUS_R: track 61.1 -> 56.8 mm
- net -15V: track 257.5 -> 259.4 mm
- net PHANTOM_PW: track 10.5 -> 9.72 mm
